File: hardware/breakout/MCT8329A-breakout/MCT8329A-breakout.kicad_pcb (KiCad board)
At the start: 2 copper layers, 23.9 x 51.9 mm, 15 parts, among them J1 Conn_01x14, J2 Conn_01x20, U1 MCT8329A

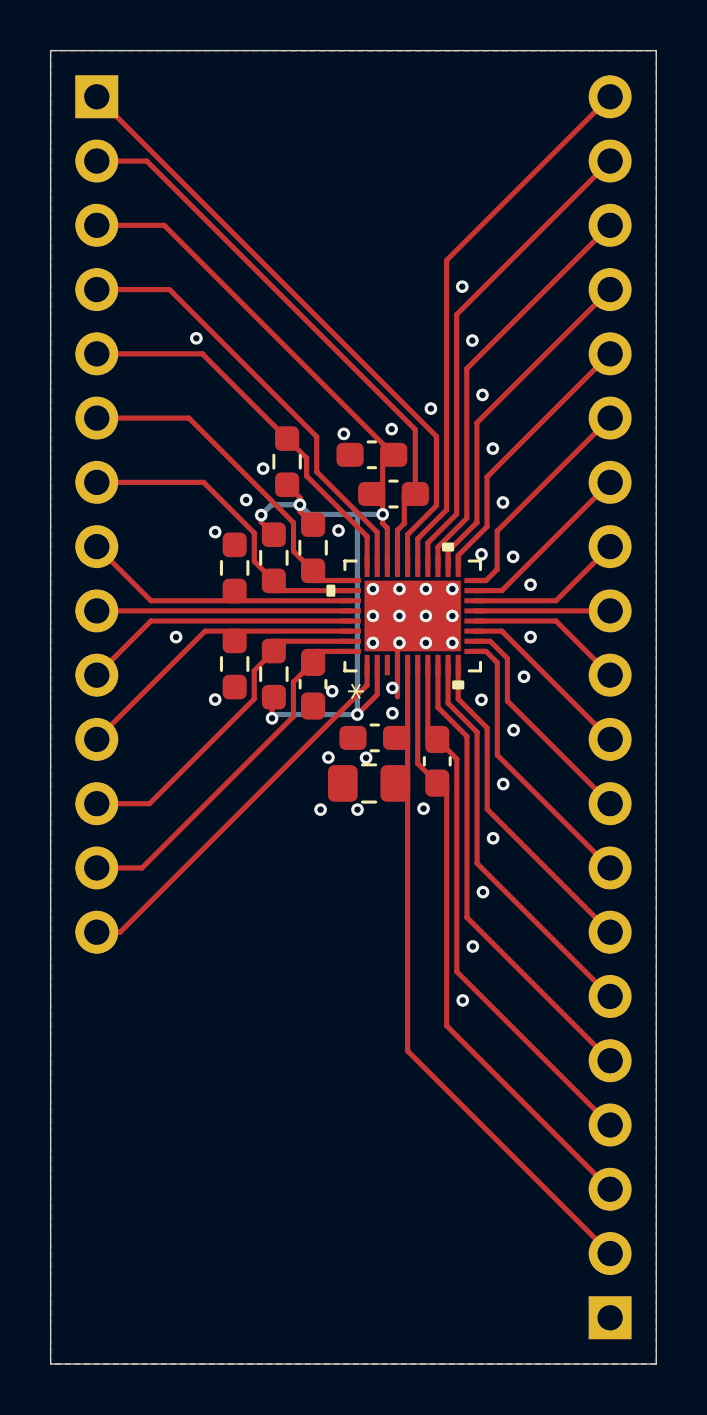
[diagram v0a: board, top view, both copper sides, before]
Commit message: Finish ooard setup and add pin labels.
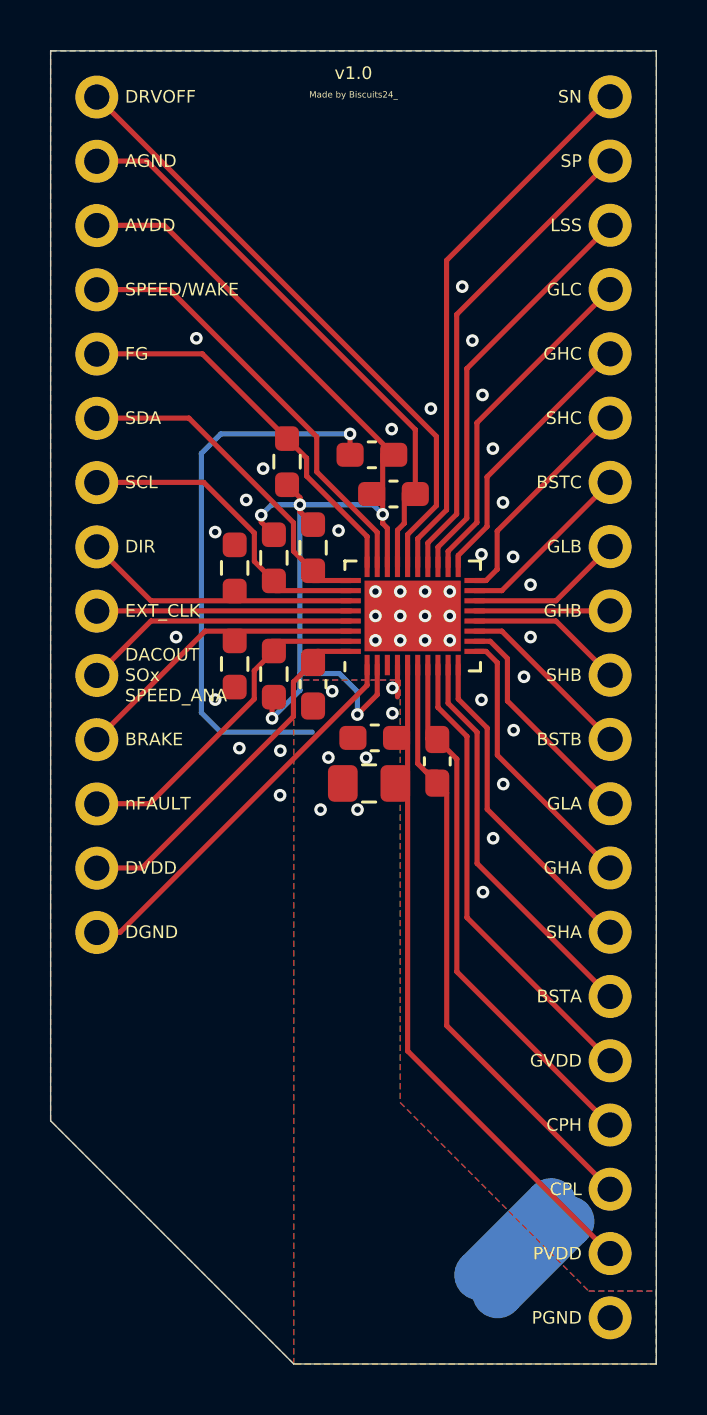
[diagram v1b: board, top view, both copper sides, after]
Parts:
- added NT1: NetTie_2, NetTie:NetTie-2_SMD_Pad2.0mm, B.Cu at (149.8, 105.9)
- added NT1: NetTie_2, NetTie:NetTie-2_SMD_Pad2.0mm, B.Cu at (149.1, 105.2)
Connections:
- net /NFAULT renamed /nFAULT
- C1 pad 2: GND -> PGND
- C2 pad 2: GND -> PGND
- C4 pad 2: GND -> PGND
- C5 pad 2: GND -> PGND
- J2 pad 1: GND -> PGND
- U1 pad 4: GND -> PGND
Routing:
- net PGND: track 0.00 -> 23.2 mm, vias 0 -> 8
- net GND: track 2.40 -> 0.00 mm, vias 47 -> 39
- net AVDD: track 42.5 -> 43.5 mm
- net /CPL: track 23.7 -> 24.3 mm
- added copper zone on B.Cu, net PGND
- added copper zone on F.Cu, net PGND
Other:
- outline, holes or cut-outs redrawn
- board text added: "AGND"
- board text added: "AVDD"
- board text added: "BRAKE"
- board text added: "BSTA"
- board text added: "BSTB"
- board text added: "BSTC"
- board text added: "CPH"
- board text added: "CPL"
- board text added: "DACOUT SOx SPEED_ANA"
- board text added: "DGND"
- board text added: "DIR"
- board text added: "DRVOFF"
- board text added: "DVDD"
- board text added: "EXT_CLK"
- board text added: "FG"
- board text added: "GHA"
- board text added: "GHB"
- board text added: "GHC"
- board text added: "GLA"
- board text added: "GLB"
- board text added: "GLC"
- board text added: "GVDD"
- board text added: "LSS"
- board text added: "Made by Biscuits24_"
- board text added: "PGND"
- board text added: "PVDD"
- board text added: "SCL"
- board text added: "SDA"
- board text added: "SHA"
- board text added: "SHB"
- board text added: "SHC"
- board text added: "SN"
- board text added: "SP"
- board text added: "SPEED/WAKE"
- board text added: "nFAULT"
- board text added: "v1.0"
